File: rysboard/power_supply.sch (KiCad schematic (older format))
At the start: 34 parts, among them J19 Fan_Connector, Q1 DMP3036SSD-13, Q3 NST847BDP6T5G, Q4 NST847BDP6T5G, Q5 DMP3036SSD-13, U3 ST1S10, U6 L78L33_SO8

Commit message: stm scheeme
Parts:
- removed U6: L78L33_SO8, Package_SO:SOIC-8_3.9x4.9mm_P1.27mm, symbol Regulator_Linear:L78L33_SO8
- added U10: L78L33_SOT89, Package_TO_SOT_SMD:SOT-89-3, symbol Regulator_Linear:L78L33_SOT89
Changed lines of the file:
@@
 12.6V Constant Current / Constant Voltage Supply\n\n
-$Comp
-L Regulator_Linear:L78L33_SO8 U6
-U 1 1 5FD37A28
-P 3150 6850
-F 0 "U6" H 3150 7092 50  0000 C CNN
-F 1 "L78L33_SO8" H 3150 7001 50  0000 C CNN
-F 2 "Package_SO:SOIC-8_3.9x4.9mm_P1.27mm" H 3250 7050 50  0001 C CIN
-F 3 "http://www.st.com/content/ccc/resource/technical/document/datasheet/15/55/e5/aa/23/5b/43/fd/CD00000446.pdf/files/CD00000446.pdf/jcr:content/translations/en.CD00000446.pdf" H 3350 6850 50  0001 C CNN
-	1    3150 6850
-	1    0    0    -1
-$EndComp
 $Comp
 L Device:C C?
@@
 	1    0    0    -1
 $EndComp
-Wire Wire Line
-	3750 7150 3150 7150
-Connection ~ 3150 7150
-Wire Wire Line
-	3150 7150 2550 7150
 Wire Wire Line
 	2550 6850 2850 6850
@@
 Text Label 2525 3925 3    50   ~ 0
 Fan_12V
+$Comp
+L Regulator_Linear:L78L33_SOT89 U10
+U 1 1 605FC97E
+P 3150 6850
+F 0 "U10" H 3150 7092 50  0000 C CNN
+F 1 "L78L33_SOT89" H 3150 7001 50  0000 C CNN
+F 2 "Package_TO_SOT_SMD:SOT-89-3" H 3150 7050 50  0001 C CIN
+F 3 "http://www.st.com/content/ccc/resource/technical/document/datasheet/15/55/e5/aa/23/5b/43/fd/CD00000446.pdf/files/CD00000446.pdf/jcr:content/translations/en.CD00000446.pdf" H 3150 6800 50  0001 C CNN
+	1    3150 6850
+	1    0    0    -1
+$EndComp
+Wire Wire Line
+	2550 7150 3150 7150
+Connection ~ 3150 7150
+Wire Wire Line
+	3150 7150 3750 7150
 $EndSCHEMATC

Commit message: mcu IO
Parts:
- renumbered Q3 to Q7
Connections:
- net ENABLE_RAIL_12V: now reaches R8.1
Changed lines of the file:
@@
 F0 "Batterry_Charging_Powes_Spply" 50
 F1 "batterry_charging_power_upply.sch" 50
-F2 "ENABLE_CHARGING" I L 7400 4300 50
-F3 "CHG_CURRENT" O L 7400 4500 50
+F2 "CHG_CURRENT" O L 7400 4500 50
 $EndSheet
 $Comp
@@
 $EndComp
 $Comp
-L rysboard:NST847BDP6T5G Q3
+L rysboard:NST847BDP6T5G Q7
 U 1 1 606E8E92
 P 2175 4525
-F 0 "Q3" H 2365 4571 50  0000 L CNN
+F 0 "Q7" H 2365 4571 50  0000 L CNN
 F 1 "NST847BDP6T5G" H 2365 4480 50  0000 L CNN
 F 2 "Package_TO_SOT_SMD:SOT-963" H 2375 4625 50  0001 C CNN
@@
 Wire Wire Line
 	2550 6625 2550 6850
-Text HLabel 7250 4300 0    50   Output ~ 0
-ENABLE_CHARGING
-Wire Wire Line
-	7250 4300 7400 4300
 $Comp
 L Device:D_Zener D14
@@
 Wire Wire Line
 	3150 7150 3750 7150
+Text HLabel 3050 1875 0    50   Output ~ 0
+ENABLE_RAIL_12V
 $EndSCHEMATC

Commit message: MCU Sensors Done
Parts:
- removed C19: 10n, Capacitor_SMD:C_0603_1608Metric, symbol Device:C
- removed C22: 100n, Capacitor_SMD:C_0603_1608Metric, symbol Device:C
- removed U10: L78L33_SOT89, Package_TO_SOT_SMD:SOT-89-3, symbol Regulator_Linear:L78L33_SOT89
- added U6: AP7381-33SA-7, Package_TO_SOT_SMD:SOT-23, symbol Reference_Voltage:MAX6035xxUR50
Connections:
- net GND: now also U6.3 (GND)
- net MCU_3.3V: now also U6.2 (OUT)
- net at C15.1, D5.1, D6.1: now also U6.1 (IN)
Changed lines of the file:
@@
 $EndComp
-Wire Wire Line
-	2550 6850 2850 6850
 Wire Wire Line
 	3450 6850 3750 6850
@@
 Connection ~ 2550 7150
 Wire Wire Line
-	10475 1350 10700 1350
-Connection ~ 10475 1350
-Wire Wire Line
 	9175 1550 9575 1550
 Connection ~ 9575 1350
@@
 	9575 1350 9875 1350
 Wire Wire Line
-	9575 2150 9875 2150
-Wire Wire Line
 	9875 1350 10175 1350
 Wire Wire Line
 	9875 2150 10175 2150
-Wire Wire Line
-	10175 2150 10475 2150
-Wire Wire Line
-	9175 2150 9575 2150
-Wire Wire Line
-	10475 2150 10700 2150
-Connection ~ 10475 2150
 Connection ~ 10175 2150
-Wire Wire Line
-	10175 1350 10475 1350
 Connection ~ 10175 1350
 Connection ~ 9875 2150
 Connection ~ 9875 1350
-Connection ~ 9575 2150
-$Comp
-L Device:C C?
-U 1 1 5EC0EC4E
-P 9575 1800
-AR Path="/5EB7428E/5EC0EC4E" Ref="C?"  Part="1"
-AR Path="/5E8FCBC6/5EC0EC4E" Ref="C19"  Part="1"
-F 0 "C19" H 9475 1875 50  0000 L CNN
-F 1 "10n" H 9550 1750 50  0000 R TNN
-F 2 "Capacitor_SMD:C_0603_1608Metric" H 9613 1650 50  0001 C CNN
-F 3 "~" H 9575 1800 50  0001 C CNN
-	1    9575 1800
-	1    0    0    -1
-$EndComp
 $Comp
 L Device:C C?
@@
 	1    0    0    -1
 $EndComp
-$Comp
-L Device:C C?
-U 1 1 5EC37980
-P 10475 1800
-AR Path="/5EB7428E/5EC37980" Ref="C?"  Part="1"
-AR Path="/5E8FCBC6/5EC37980" Ref="C22"  Part="1"
-F 0 "C22" H 10475 1925 60  0000 R TNN
-F 1 "100n" H 10475 1750 60  0000 R TNN
-F 2 "Capacitor_SMD:C_0603_1608Metric" H 10375 1890 60  0001 C CNN
-F 3 "~" H 10375 1890 60  0001 C CNN
-	1    10475 1800
-	1    0    0    -1
-$EndComp
 Wire Wire Line
 	9575 1550 9575 1350
 Wire Wire Line
-	9575 1650 9575 1550
-Connection ~ 9575 1550
-Wire Wire Line
 	9875 1350 9875 1650
 Wire Wire Line
 	10175 1350 10175 1650
 Wire Wire Line
-	10475 1350 10475 1650
-Wire Wire Line
-	9575 2150 9575 1950
-Wire Wire Line
 	9875 2150 9875 1950
 Wire Wire Line
 	10175 2150 10175 1950
-Wire Wire Line
-	10475 2150 10475 1950
 $Comp
 L Device:LED D9
@@
 	1    0    0    -1
 $EndComp
-Connection ~ 2550 6850
 Text Notes 2725 825  0    50   ~ 0
 Reverse Polarrity Protection and fuse\nMust be rated for 14A.\n
@@
 F0 "Batterry_Charging_Powes_Spply" 50
 F1 "batterry_charging_power_upply.sch" 50
-F2 "CHG_CURRENT" O L 7400 4500 50
 $EndSheet
 $Comp
@@
 	2400 6200 2550 6200
 Wire Wire Line
-	2550 6200 2550 6625
+	2550 6200 2550 6550
 Wire Wire Line
 	2400 6625 2550 6625
@@
 	0    1    1    0
 $EndComp
-Text HLabel 7250 4500 0    50   Input ~ 0
-CHG_CURRENT
-Wire Wire Line
-	7250 4500 7400 4500
 Text HLabel 2175 3450 2    50   Input ~ 0
 FAN_TACHOMETER
@@
 Text Label 2525 3925 3    50   ~ 0
 Fan_12V
-$Comp
-L Regulator_Linear:L78L33_SOT89 U10
-U 1 1 605FC97E
-P 3150 6850
-F 0 "U10" H 3150 7092 50  0000 C CNN
-F 1 "L78L33_SOT89" H 3150 7001 50  0000 C CNN
-F 2 "Package_TO_SOT_SMD:SOT-89-3" H 3150 7050 50  0001 C CIN
-F 3 "http://www.st.com/content/ccc/resource/technical/document/datasheet/15/55/e5/aa/23/5b/43/fd/CD00000446.pdf/files/CD00000446.pdf/jcr:content/translations/en.CD00000446.pdf" H 3150 6800 50  0001 C CNN
-	1    3150 6850
-	1    0    0    -1
-$EndComp
-Wire Wire Line
-	2550 7150 3150 7150
-Connection ~ 3150 7150
-Wire Wire Line
-	3150 7150 3750 7150
 Text HLabel 3050 1875 0    50   Output ~ 0
 ENABLE_RAIL_12V
+$Comp
+L Reference_Voltage:MAX6035xxUR50 U6
+U 1 1 60692F05
+P 3150 6850
+F 0 "U6" H 2921 6896 50  0000 R CNN
+F 1 "AP7381-33SA-7 " H 2921 6805 50  0000 R CNN
+F 2 "Package_TO_SOT_SMD:SOT-23" H 3250 6550 50  0001 C CIN
+F 3 "https://datasheets.maximintegrated.com/en/ds/MAX6035.pdf" H 3250 6500 50  0001 C CIN
+	1    3150 6850
+	1    0    0    -1
+$EndComp
+Wire Wire Line
+	2550 7150 3050 7150
+Connection ~ 3050 7150
+Wire Wire Line
+	3050 7150 3750 7150
+Wire Wire Line
+	3050 6550 2550 6550
+Connection ~ 2550 6550
+Wire Wire Line
+	2550 6550 2550 6625
+Wire Wire Line
+	10175 2150 10700 2150
+Wire Wire Line
+	10175 1350 10700 1350
+Wire Wire Line
+	9175 2150 9875 2150
 $EndSCHEMATC

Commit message: Bom finished pcb cleanup started
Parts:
- removed D14, D3: TSZU52C10 RG, Diode_SMD:D_0603_1608Metric, symbol Device:D_Zener
- removed unit 2 of Q1
- removed unit 1 of Q4
- removed R10: 110KR, Resistor_SMD:R_0603_1608Metric, symbol Device:R
- removed R8: 10k, Resistor_SMD:R_0603_1608Metric, symbol Device:R
- added D4: SZ1SMA15CAT3G, Diode_SMD:D_SMA_Handsoldering, symbol Device:D_Zener
- D13: value TSZU52C10 RG -> SZ1SMA15CAT3G; footprint Diode_SMD:D_0603_1608Metric -> Diode_SMD:D_SMA_Handsoldering
- U3: footprint Package_SO:TI_SO-PowerPAD-8 -> Package_DFN_QFN:DFN-8-1EP_4x4mm_P0.8mm_EP2.3x3.24mm
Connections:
- net +12V: now also D4.1 (K)
- net at Q1.2 (G1), Q4.3 (C2), R12.2: now also D4.2 (A)
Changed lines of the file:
@@
 F 0 "U3" H 8275 1792 50  0000 C CNN
 F 1 "ST1S10" H 8275 1701 50  0000 C CNN
-F 2 "Package_SO:TI_SO-PowerPAD-8" H 8400 1100 50  0001 L CIN
+F 2 "Package_DFN_QFN:DFN-8-1EP_4x4mm_P0.8mm_EP2.3x3.24mm" H 8400 1100 50  0001 L CIN
 F 3 "http://www.st.com/internet/com/TECHNICAL_RESOURCES/TECHNICAL_LITERATURE/DATASHEET/CD00169322.pdf" H 8275 1450 50  0001 C CNN
 F 4 " ST1S10PHR" H 8275 1450 50  0001 C CNN "PartID"
@@
 F5 "PACK+" O R 1675 1175 50
 F6 "PACK-" I R 1675 1825 50
+F7 "EN_12V" I R 1675 1625 50
 $EndSheet
 Wire Wire Line
@@
 F1 "batterry_charging_power_upply.sch" 50
 $EndSheet
-$Comp
-L power:+BATT #PWR034
-U 1 1 605BC324
-P 2150 1175
-F 0 "#PWR034" H 2150 1025 50  0001 C CNN
-F 1 "+BATT" H 2165 1348 50  0000 C CNN
-F 2 "" H 2150 1175 50  0001 C CNN
-F 3 "" H 2150 1175 50  0001 C CNN
-	1    2150 1175
-	1    0    0    -1
-$EndComp
 $Comp
 L power:+5V #PWR038
@@
 Wire Wire Line
 	2550 6625 2550 6850
-$Comp
-L Device:D_Zener D14
-U 1 1 604A195B
-P 5400 1500
-F 0 "D14" V 5325 1125 50  0000 L CNN
-F 1 "TSZU52C10 RG" V 5475 875 50  0000 L CNN
-F 2 "Diode_SMD:D_0603_1608Metric" H 5400 1500 50  0001 C CNN
-F 3 "~" H 5400 1500 50  0001 C CNN
-	1    5400 1500
-	0    1    1    0
-$EndComp
 Wire Wire Line
 	5400 1650 5600 1650
@@
 P 1575 4100
 F 0 "D13" V 1500 3675 50  0000 L CNN
-F 1 "TSZU52C10 RG" V 1625 3425 50  0000 L CNN
-F 2 "Diode_SMD:D_0603_1608Metric" H 1575 4100 50  0001 C CNN
+F 1 "SZ1SMA15CAT3G" V 1625 3425 50  0000 L CNN
+F 2 "Diode_SMD:D_SMA_Handsoldering" H 1575 4100 50  0001 C CNN
 F 3 "~" H 1575 4100 50  0001 C CNN
 	1    1575 4100
@@
 	1    0    0    -1
 $EndComp
-Connection ~ 5400 1350
 $Comp
 L Device:C C?
@@
 	2175 1825 1675 1825
 $Comp
-L rysboard:DMP3036SSD-13 Q1
-U 2 1 60615F71
-P 3650 1275
-F 0 "Q1" V 3992 1275 50  0000 C CNN
-F 1 "DMP3036SSD-13" V 3901 1275 50  0000 C CNN
-F 2 "Package_SO:SO-8_3.9x4.9mm_P1.27mm" H 3850 1200 50  0001 L CIN
-F 3 "" H 3650 1275 50  0001 L CNN
-	2    3650 1275
-	0    1    -1   0
-$EndComp
-$Comp
-L Device:D_Zener D3
-U 1 1 60616F79
-P 2925 1325
-F 0 "D3" V 2850 950 50  0000 L CNN
-F 1 "TSZU52C10 RG" V 3000 700 50  0000 L CNN
-F 2 "Diode_SMD:D_0603_1608Metric" H 2925 1325 50  0001 C CNN
-F 3 "~" H 2925 1325 50  0001 C CNN
-	1    2925 1325
-	0    1    1    0
-$EndComp
-$Comp
-L Device:R R10
-U 1 1 606173BC
-P 3225 1325
-F 0 "R10" H 3295 1371 50  0000 L CNN
-F 1 "110KR" H 3295 1280 50  0000 L CNN
-F 2 "Resistor_SMD:R_0603_1608Metric" V 3155 1325 50  0001 C CNN
-F 3 "~" H 3225 1325 50  0001 C CNN
-	1    3225 1325
-	1    0    0    -1
-$EndComp
-$Comp
-L rysboard:NST847BDP6T5G Q4
-U 1 1 6061762B
-P 3550 1875
-F 0 "Q4" H 3740 1921 50  0000 L CNN
-F 1 "NST847BDP6T5G" H 3740 1830 50  0000 L CNN
-F 2 "Package_TO_SOT_SMD:SOT-963" H 3750 1975 50  0001 C CNN
-F 3 "~" H 3550 1875 50  0001 C CNN
-	1    3550 1875
-	1    0    0    -1
-$EndComp
-$Comp
-L Device:R R8
-U 1 1 60617A11
-P 3200 1875
-F 0 "R8" V 3280 1875 50  0000 C CNN
-F 1 "10k" V 3200 1875 50  0000 C CNN
-F 2 "Resistor_SMD:R_0603_1608Metric" V 3130 1875 50  0001 C CNN
-F 3 "~" H 3200 1875 50  0001 C CNN
-	1    3200 1875
-	0    -1   -1   0
-$EndComp
-$Comp
-L power:+BATT #PWR020
-U 1 1 60617D1F
-P 2925 1175
-F 0 "#PWR020" H 2925 1025 50  0001 C CNN
-F 1 "+BATT" H 2940 1348 50  0000 C CNN
-F 2 "" H 2925 1175 50  0001 C CNN
-F 3 "" H 2925 1175 50  0001 C CNN
-	1    2925 1175
-	1    0    0    -1
-$EndComp
-Wire Wire Line
-	2925 1175 3225 1175
-Connection ~ 2925 1175
-Connection ~ 3225 1175
-Wire Wire Line
-	3225 1175 3450 1175
-Wire Wire Line
-	3225 1475 3650 1475
-Connection ~ 3225 1475
-Wire Wire Line
-	3650 1475 3650 1675
-Connection ~ 3650 1475
-$Comp
-L power:GND #PWR024
-U 1 1 606277F2
-P 3650 2075
-F 0 "#PWR024" H 3650 1825 50  0001 C CNN
-F 1 "GND" H 3655 1902 50  0000 C CNN
-F 2 "" H 3650 2075 50  0001 C CNN
-F 3 "" H 3650 2075 50  0001 C CNN
-	1    3650 2075
-	1    0    0    -1
-$EndComp
-$Comp
 L power:+12V #PWR035
 U 1 1 60627A51
-P 4125 1175
-F 0 "#PWR035" H 4125 1025 50  0001 C CNN
-F 1 "+12V" H 4140 1348 50  0000 C CNN
-F 2 "" H 4125 1175 50  0001 C CNN
-F 3 "" H 4125 1175 50  0001 C CNN
-	1    4125 1175
-	1    0    0    -1
-$EndComp
-Wire Wire Line
-	4125 1175 3850 1175
+P 2150 1175
+F 0 "#PWR035" H 2150 1025 50  0001 C CNN
+F 1 "+12V" H 2165 1348 50  0000 C CNN
+F 2 "" H 2150 1175 50  0001 C CNN
+F 3 "" H 2150 1175 50  0001 C CNN
+	1    2150 1175
+	1    0    0    -1
+$EndComp
 Connection ~ 6000 1650
-Wire Wire Line
-	2925 1475 3225 1475
 Text Label 8800 1350 0    50   ~ 0
 SW
@@
 Text Label 2525 3925 3    50   ~ 0
 Fan_12V
-Text HLabel 3050 1875 0    50   Output ~ 0
+Text HLabel 2175 1625 2    50   Output ~ 0
 ENABLE_RAIL_12V
 $Comp
@@
 Wire Wire Line
 	9175 2150 9875 2150
+$Comp
+L Device:D_Zener D4
+U 1 1 608D62AB
+P 5400 1500
+F 0 "D4" V 5325 1125 50  0000 L CNN
+F 1 "SZ1SMA15CAT3G" V 5475 875 50  0000 L CNN
+F 2 "Diode_SMD:D_SMA_Handsoldering" H 5400 1500 50  0001 C CNN
+F 3 "~" H 5400 1500 50  0001 C CNN
+	1    5400 1500
+	0    1    1    0
+$EndComp
+Connection ~ 5400 1350
+Wire Wire Line
+	2175 1625 1675 1625
 $EndSCHEMATC

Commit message: bom + excel ready
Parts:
- removed D13, D4: SZ1SMA15CAT3G, Diode_SMD:D_SMA_Handsoldering, symbol Device:D_Zener
- removed Q5: DMP3036SSD-13, Package_SO:SO-8_3.9x4.9mm_P1.27mm, symbol rysboard:DMP3036SSD-13
- added Q?: PMV28XPEAR, Package_TO_SOT_SMD:SOT-23, symbol Transistor_FET:AO3401A
- added R?: 1k, Resistor_SMD:R_0603_1608Metric, symbol Device:R
- R11: value 10k -> 10k1%
- R7: value 10KR -> 10k1%
- renumbered Q1 to Q5
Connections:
- net +12V: now also Q?.2 (S)
- net Fan_12V: now also Q?.3 (D)
- net at R7.2: now also Q?.1 (G), R?.1; no longer Q7.6 (C1)
- new net: Q7.6 (C1), R?.2
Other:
- moved on the sheet: Q7A, R9
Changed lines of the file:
@@
 P 5550 1950
 F 0 "R11" V 5630 1950 50  0000 C CNN
-F 1 "10k" V 5550 1950 50  0000 C CNN
+F 1 "10k1%" V 5550 1950 50  0000 C CNN
 F 2 "Resistor_SMD:R_0603_1608Metric" V 5480 1950 50  0001 C CNN
 F 3 "~" H 5550 1950 50  0001 C CNN
@@
 L Device:R R9
 U 1 1 606033C9
-P 1825 4525
-F 0 "R9" V 1905 4525 50  0000 C CNN
-F 1 "1k" V 1825 4525 50  0000 C CNN
-F 2 "Resistor_SMD:R_0603_1608Metric" V 1755 4525 50  0001 C CNN
-F 3 "~" H 1825 4525 50  0001 C CNN
-	1    1825 4525
+P 1825 4825
+F 0 "R9" V 1905 4825 50  0000 C CNN
+F 1 "1k" V 1825 4825 50  0000 C CNN
+F 2 "Resistor_SMD:R_0603_1608Metric" V 1755 4825 50  0001 C CNN
+F 3 "~" H 1825 4825 50  0001 C CNN
+	1    1825 4825
 	0    -1   -1   0
 $EndComp
@@
 L power:GND #PWR031
 U 1 1 60603989
-P 2275 4725
-F 0 "#PWR031" H 2275 4475 50  0001 C CNN
-F 1 "GND" H 2280 4552 50  0000 C CNN
-F 2 "" H 2275 4725 50  0001 C CNN
-F 3 "" H 2275 4725 50  0001 C CNN
-	1    2275 4725
+P 2275 5025
+F 0 "#PWR031" H 2275 4775 50  0001 C CNN
+F 1 "GND" H 2280 4852 50  0000 C CNN
+F 2 "" H 2275 5025 50  0001 C CNN
+F 3 "" H 2275 5025 50  0001 C CNN
+	1    2275 5025
 	1    0    0    -1
 $EndComp
@@
 P 1825 4125
 F 0 "R7" H 1895 4171 50  0000 L CNN
-F 1 "10KR" H 1895 4080 50  0000 L CNN
+F 1 "10k1%" H 1895 4080 50  0000 L CNN
 F 2 "Resistor_SMD:R_0603_1608Metric" V 1755 4125 50  0001 C CNN
 F 3 "~" H 1825 4125 50  0001 C CNN
@@
 Text HLabel 5400 1950 0    50   Output ~ 0
 ENABLE_RAIL_5V
-Text HLabel 1675 4525 0    50   Output ~ 0
+Text HLabel 1675 4825 0    50   Output ~ 0
 PWM_FAN
 $Comp
@@
 L rysboard:NST847BDP6T5G Q7
 U 1 1 606E8E92
-P 2175 4525
-F 0 "Q7" H 2365 4571 50  0000 L CNN
-F 1 "NST847BDP6T5G" H 2365 4480 50  0000 L CNN
-F 2 "Package_TO_SOT_SMD:SOT-963" H 2375 4625 50  0001 C CNN
-F 3 "~" H 2175 4525 50  0001 C CNN
-	1    2175 4525
+P 2175 4825
+F 0 "Q7" H 2365 4871 50  0000 L CNN
+F 1 "NST847BDP6T5G" H 2365 4780 50  0000 L CNN
+F 2 "Package_TO_SOT_SMD:SOT-963" H 2375 4925 50  0001 C CNN
+F 3 "~" H 2175 4825 50  0001 C CNN
+	1    2175 4825
 	1    0    0    -1
 $EndComp
@@
 $Comp
 L rysboard:DMP3036SSD-13 Q5
-U 1 1 6051EA37
-P 2275 4025
-F 0 "Q5" V 2617 4025 50  0000 C CNN
-F 1 "DMP3036SSD-13" V 2526 4025 50  0000 C CNN
-F 2 "Package_SO:SO-8_3.9x4.9mm_P1.27mm" H 2475 3950 50  0001 L CIN
-F 3 "" H 2275 4025 50  0001 L CNN
-	1    2275 4025
-	0    1    -1   0
-$EndComp
-$Comp
-L rysboard:DMP3036SSD-13 Q1
 U 1 1 605FF267
 P 6000 1450
-F 0 "Q1" V 6342 1450 50  0000 C CNN
+F 0 "Q5" V 6342 1450 50  0000 C CNN
 F 1 "DMP3036SSD-13" V 6251 1450 50  0000 C CNN
 F 2 "Package_SO:SO-8_3.9x4.9mm_P1.27mm" H 6200 1375 50  0001 L CIN
@@
 	2550 6625 2550 6850
 Wire Wire Line
-	5400 1650 5600 1650
-Connection ~ 5600 1650
-$Comp
-L Device:D_Zener D13
-U 1 1 604A5F28
-P 1575 4100
-F 0 "D13" V 1500 3675 50  0000 L CNN
-F 1 "SZ1SMA15CAT3G" V 1625 3425 50  0000 L CNN
-F 2 "Diode_SMD:D_SMA_Handsoldering" H 1575 4100 50  0001 C CNN
-F 3 "~" H 1575 4100 50  0001 C CNN
-	1    1575 4100
-	0    1    1    0
-$EndComp
-Wire Wire Line
-	1575 4250 1575 4275
-Wire Wire Line
-	1575 4275 1825 4275
-Connection ~ 1825 4275
-Wire Wire Line
 	1575 3950 1575 3925
 Wire Wire Line
@@
 	4500 2975 4500 5050
 Wire Notes Line
-	4500 5050 550  5050
+	4525 5250 575  5250
 Wire Notes Line
 	550  5050 550  2975
@@
 Wire Wire Line
 	9175 2150 9875 2150
-$Comp
-L Device:D_Zener D4
-U 1 1 608D62AB
-P 5400 1500
-F 0 "D4" V 5325 1125 50  0000 L CNN
-F 1 "SZ1SMA15CAT3G" V 5475 875 50  0000 L CNN
-F 2 "Diode_SMD:D_SMA_Handsoldering" H 5400 1500 50  0001 C CNN
-F 3 "~" H 5400 1500 50  0001 C CNN
-	1    5400 1500
-	0    1    1    0
-$EndComp
-Connection ~ 5400 1350
 Wire Wire Line
 	2175 1625 1675 1625
+$Comp
+L Transistor_FET:AO3401A Q?
+U 1 1 60967BD5
+P 2275 4025
+F 0 "Q?" V 2617 4025 50  0000 C CNN
+F 1 "PMV28XPEAR" V 2526 4025 50  0000 C CNN
+F 2 "Package_TO_SOT_SMD:SOT-23" H 2475 3950 50  0001 L CIN
+F 3 "http://www.aosmd.com/pdfs/datasheet/AO3401A.pdf" H 2275 4025 50  0001 L CNN
+	1    2275 4025
+	0    1    -1   0
+$EndComp
+$Comp
+L Device:R R?
+U 1 1 6096D04C
+P 2275 4475
+F 0 "R?" V 2355 4475 50  0000 C CNN
+F 1 "1k" V 2275 4475 50  0000 C CNN
+F 2 "Resistor_SMD:R_0603_1608Metric" V 2205 4475 50  0001 C CNN
+F 3 "~" H 2275 4475 50  0001 C CNN
+	1    2275 4475
+	1    0    0    -1
+$EndComp
 $EndSCHEMATC

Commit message: changed ST1S10 Footprint to old one
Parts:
- U3: footprint Package_DFN_QFN:DFN-8-1EP_4x4mm_P0.8mm_EP2.3x3.24mm -> Package_SO:TI_SO-PowerPAD-8
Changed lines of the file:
@@
 F 0 "U3" H 8275 1792 50  0000 C CNN
 F 1 "ST1S10" H 8275 1701 50  0000 C CNN
-F 2 "Package_DFN_QFN:DFN-8-1EP_4x4mm_P0.8mm_EP2.3x3.24mm" H 8400 1100 50  0001 L CIN
+F 2 "Package_SO:TI_SO-PowerPAD-8" H 8400 1100 50  0001 L CIN
 F 3 "http://www.st.com/internet/com/TECHNICAL_RESOURCES/TECHNICAL_LITERATURE/DATASHEET/CD00169322.pdf" H 8275 1450 50  0001 C CNN
 F 4 " ST1S10PHR" H 8275 1450 50  0001 C CNN "PartID"

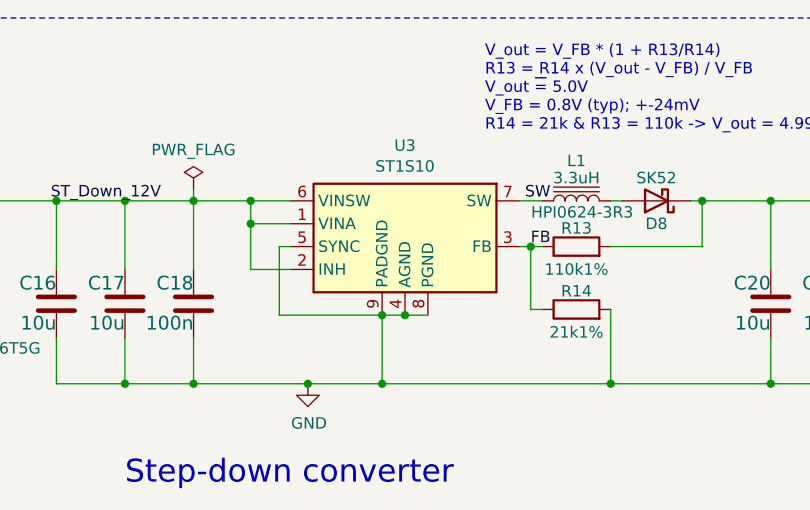
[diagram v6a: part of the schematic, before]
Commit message: removed ST1S10
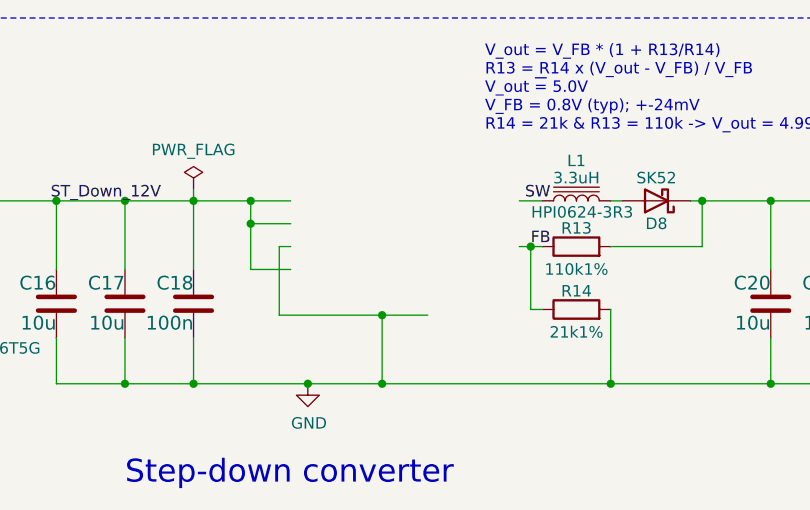
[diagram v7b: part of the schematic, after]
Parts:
- removed U3: ST1S10, Package_SO:TI_SO-PowerPAD-8, symbol Regulator_Switching:ST1S10PHR
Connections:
- wire segments 84 -> 83
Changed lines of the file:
@@
 Wire Wire Line
 	7775 1550 7725 1550
-Connection ~ 8275 1850
-Wire Wire Line
-	8175 1850 8275 1850
-Wire Wire Line
-	8375 1850 8275 1850
 Connection ~ 7050 2150
 Wire Wire Line
@@
 F 3 "~" H 6650 1890 60  0000 C CNN
 	1    6750 1800
-	1    0    0    -1
-$EndComp
-$Comp
-L Regulator_Switching:ST1S10PHR U3
-U 1 1 5E89E53A
-P 8275 1450
-F 0 "U3" H 8275 1792 50  0000 C CNN
-F 1 "ST1S10" H 8275 1701 50  0000 C CNN
-F 2 "Package_SO:TI_SO-PowerPAD-8" H 8400 1100 50  0001 L CIN
-F 3 "http://www.st.com/internet/com/TECHNICAL_RESOURCES/TECHNICAL_LITERATURE/DATASHEET/CD00169322.pdf" H 8275 1450 50  0001 C CNN
-F 4 " ST1S10PHR" H 8275 1450 50  0001 C CNN "PartID"
-F 5 "https://www.tme.eu/pl/details/st1s10phr/regulatory-napiecia-uklady-dc-dc/stmicroelectronics/" H 8275 1450 50  0001 C CNN "TME"
-	1    8275 1450
 	1    0    0    -1
 $EndComp
@@
 	1    0    0    -1
 $EndComp
+Wire Wire Line
+	8175 1850 8375 1850
 $EndSCHEMATC
